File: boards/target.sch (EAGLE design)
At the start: 20 parts, among them Q1 BC847BS, U1 MCP1703T-3002E/CB, X1 53398-04, X2 53398-04

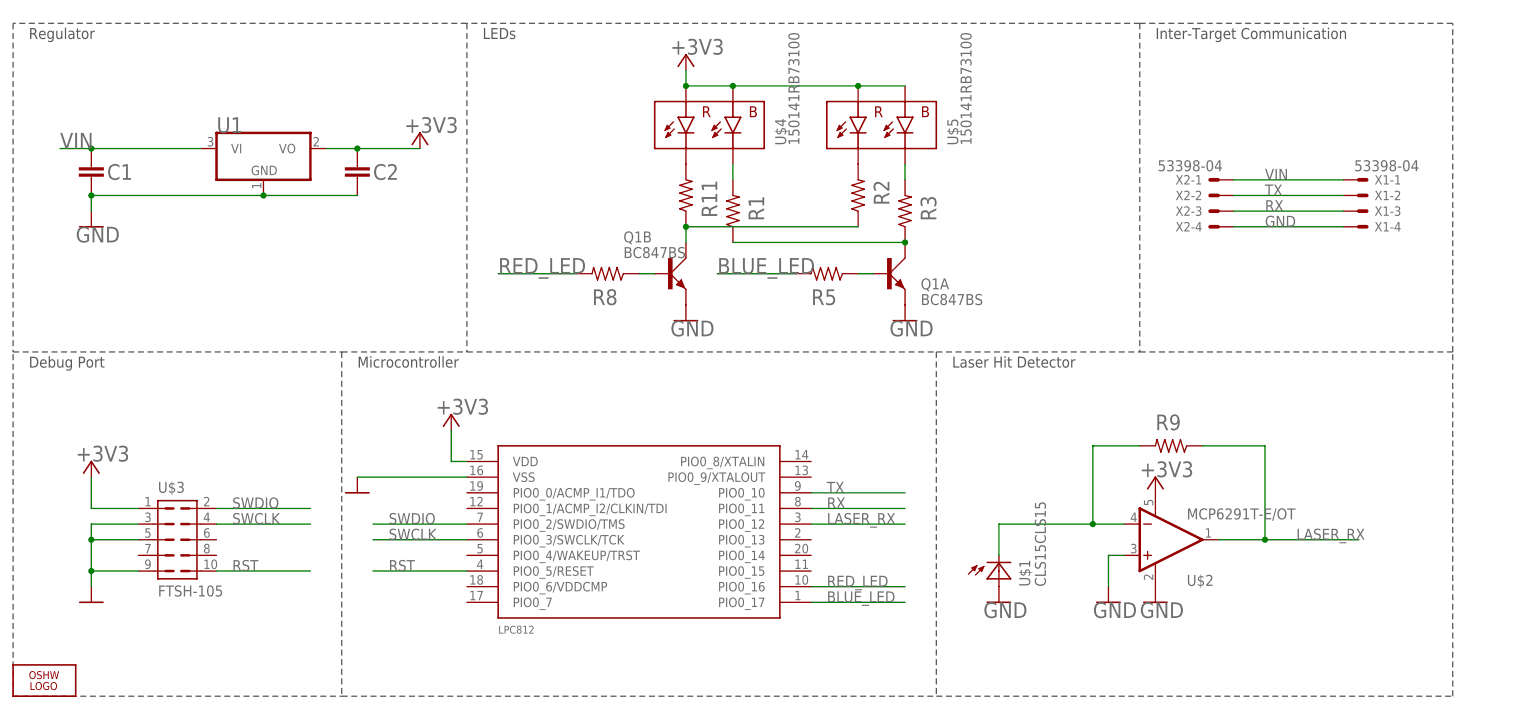
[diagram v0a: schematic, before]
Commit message: Rename to target.sch/brd. Fix controller. Add part numbers. Still needs to be routed.
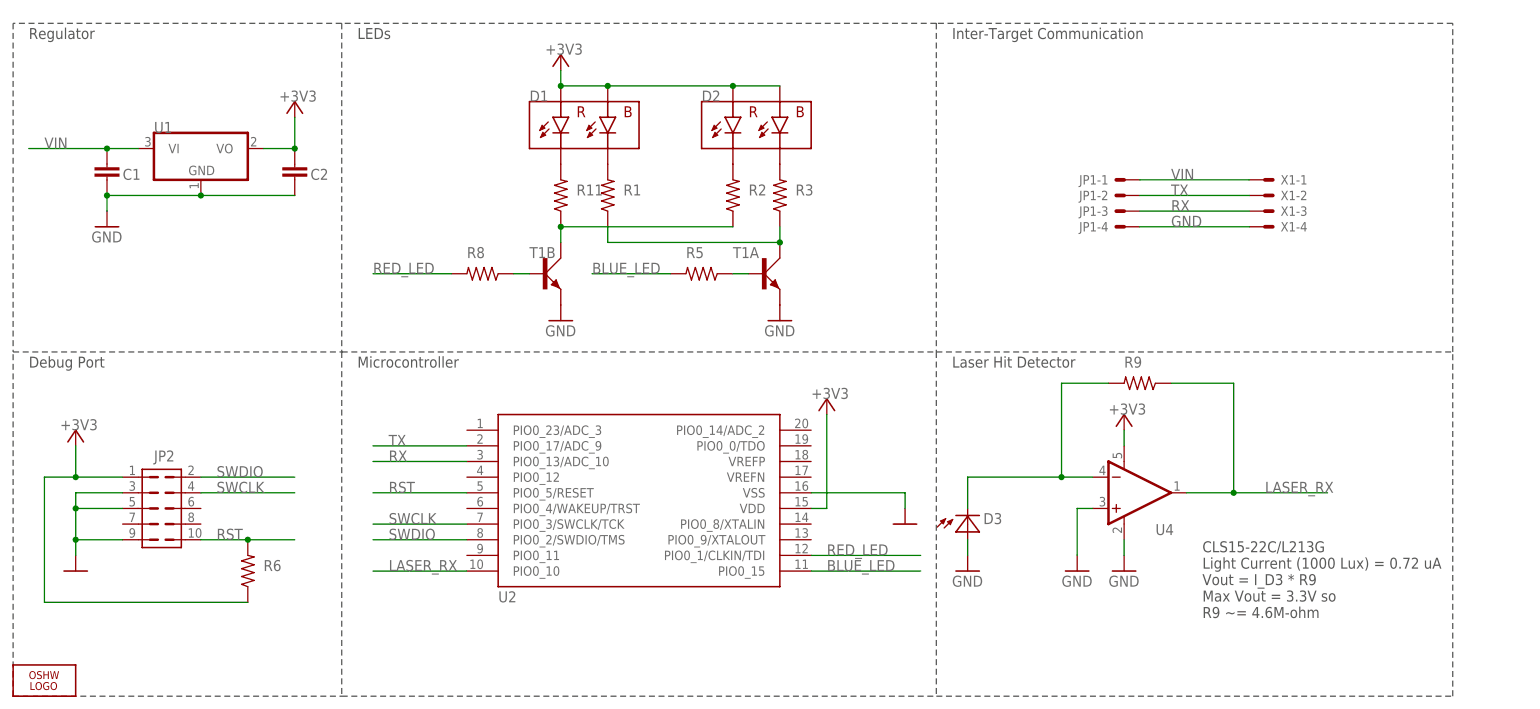
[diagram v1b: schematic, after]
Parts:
- removed LPC812: LPC812M101JDH20, LPC800:LPC812M101JDH20
- removed Q1: BC847BS, transistor-small-signal:BC847BS
- removed U$1: CLS15CLS15, torpedo:CLS15CLS15
- removed U$2: MCP6291T-E/OT, SparkFun-AnalogIC:MCP6291T-E/OT
- removed U$3: FTSH-105, torpedo:FTSH-105
- removed U$4, U$5: 150141RB73100, torpedo:LED_RB
- removed X2: 53398-04, con-molex:53398-04
- added D1, D2: 150141RB73100, torpedo:LED_RB
- added D3: 638-CLS1522CL213GTR8, torpedo:CLS15CLS15
- added JP1: 798-DF134P125V20, con-molex:53398-04
- added JP2: FTSH-105-01-L, torpedo:FTSH-105
- added R6: 71-CRCW0603-10K-E3, rcl:R-US_R0603
- added T1: 771-BC847BS-T/R, transistor-small-signal:BC847BS
- added U2: 771-LPC824M201JDH20J, torpedo:LPC824
- added U4: 579-MCP6291T-E/OT, SparkFun-AnalogIC:MCP6291T-E/OT
- R1, R3: value CRCW0603200RFKEA -> 71-CRCW0603-5.6-E3
- R11, R2: value CRCW0603200RFKEA -> 71-CRCW060368R0FKEB
- R5, R8: value CRCW0603200RFKEA -> 71-CRCW0603220RFKEB
- R9: value CRCW0603200RFKEA -> 71-CRCW06034M64FKEA
- U1: value MCP1703T-3002E/CB -> 579-MCP1703T-3002ECB
- X1: value 53398-04 -> 798-DF134P125V20
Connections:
- net +3V3: now also D1.1, D1.2, D2.1, D2.2, JP2.1, R6.1, U2.VDD, U4.V+; no longer LPC812.VDD, U$2.V+, U$3.1, U$4.1, U$4.2, U$5.1, U$5.2
- net BLUE_LED: now also U2.PIO0_15; no longer LPC812.PIO0_17
- net GND: now also D3.A, JP1-4.S, JP2.3, JP2.5, JP2.9, T1A.E, T1B.E, U2.VSS, U4.+IN, U4.V-; no longer LPC812.VSS, Q1A.E, Q1B.E, U$1.A, U$2.+IN, U$2.V-, U$3.3, U$3.5, U$3.9, X2-4.S
- net LASER_RX: now also U2.PIO0_10, U4.OUT; no longer LPC812.PIO0_12, U$2.OUT
- net N$1: now also T1A.C; no longer Q1A.C
- net N$11: now also T1B.B; no longer Q1B.B
- net N$2: now also T1B.C; no longer Q1B.C
- net N$3: now also D1.3; no longer U$4.3
- net N$4: now also T1A.B; no longer Q1A.B
- net N$5: now also D3.C, U4.-IN; no longer U$1.C, U$2.-IN
- net N$6: now also D2.3; no longer U$5.3
- net N$7: now also D1.4; no longer U$4.4
- net N$8: now also D2.4; no longer U$5.4
- net RED_LED: now also U2.PIO0_1/CLKIN/TDI; no longer LPC812.PIO0_16
- net RST: now also JP2.10, R6.2, U2.PIO0_5/RESET; no longer LPC812.PIO0_5/RESET, U$3.10
- net RX: now also JP1-3.S, U2.PIO0_13/ADC_10; no longer LPC812.PIO0_11, X2-3.S
- net SWCLK: now also JP2.4, U2.PIO0_3/SWCLK/TCK; no longer LPC812.PIO0_3/SWCLK/TCK, U$3.4
- net SWDIO: now also JP2.2, U2.PIO0_2/SWDIO/TMS; no longer LPC812.PIO0_2/SWDIO/TMS, U$3.2
- net TX: now also JP1-2.S, U2.PIO0_17/ADC_9; no longer LPC812.PIO0_10, X2-2.S
- net VIN: now also JP1-1.S; no longer X2-1.S
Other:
- note added: "CLS15-22C/L213G Light Current (1000 Lux) = 0.72 uA Vout = I_D3 * R9 Max Vout = 3.3V so R9 ~= 4.6M-ohm"
- moved on the sheet: C1, C2, R1, R11, R2, R3, R5, R8, R9, U1, X1-1, X1-2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

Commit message: Working on target layout
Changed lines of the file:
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@@
 <part name="JP2" library="torpedo" deviceset="FTSH-105" device="" value="FTSH-105-01-L"/>
 <part name="R6" library="rcl" deviceset="R-US_" device="R0603" value="71-CRCW0603-10K-E3"/>
+<part name="GND3" library="supply1" deviceset="GND" device=""/>
+<part name="GND10" library="supply1" deviceset="GND" device=""/>
 </parts>
 <sheets>
@@
 <attribute name="NAME" x="40.64" y="20.32" size="1.778" layer="95"/>
 </instance>
+<instance part="GND3" gate="1" x="30.48" y="76.2" smashed="yes">
+<attribute name="VALUE" x="27.94" y="73.66" size="1.778" layer="96"/>
+</instance>
+<instance part="GND10" gate="1" x="45.72" y="76.2" smashed="yes">
+<attribute name="VALUE" x="43.18" y="73.66" size="1.778" layer="96"/>
+</instance>
 </instances>
 <busses>
@@
 <net name="GND" class="0">
 <segment>
+<pinref part="C1" gate="G$1" pin="2"/>
 <pinref part="GND1" gate="1" pin="GND"/>
 <wire x1="15.24" y1="78.74" x2="15.24" y2="81.28" width="0.1524" layer="91"/>
-<pinref part="U1" gate="G$1" pin="GND"/>
-<wire x1="15.24" y1="81.28" x2="30.48" y2="81.28" width="0.1524" layer="91"/>
-<pinref part="C1" gate="G$1" pin="2"/>
-<junction x="15.24" y="81.28"/>
-<pinref part="C2" gate="G$1" pin="2"/>
-<wire x1="30.48" y1="81.28" x2="45.72" y2="81.28" width="0.1524" layer="91"/>
-<junction x="30.48" y="81.28"/>
 </segment>
 <segment>
@@
 <junction x="10.16" y="25.4"/>
 </segment>
+<segment>
+<pinref part="U1" gate="G$1" pin="GND"/>
+<pinref part="GND3" gate="1" pin="GND"/>
+<wire x1="30.48" y1="81.28" x2="30.48" y2="78.74" width="0.1524" layer="91"/>
+</segment>
+<segment>
+<pinref part="C2" gate="G$1" pin="2"/>
+<pinref part="GND10" gate="1" pin="GND"/>
+<wire x1="45.72" y1="81.28" x2="45.72" y2="78.74" width="0.1524" layer="91"/>
+</segment>
 </net>

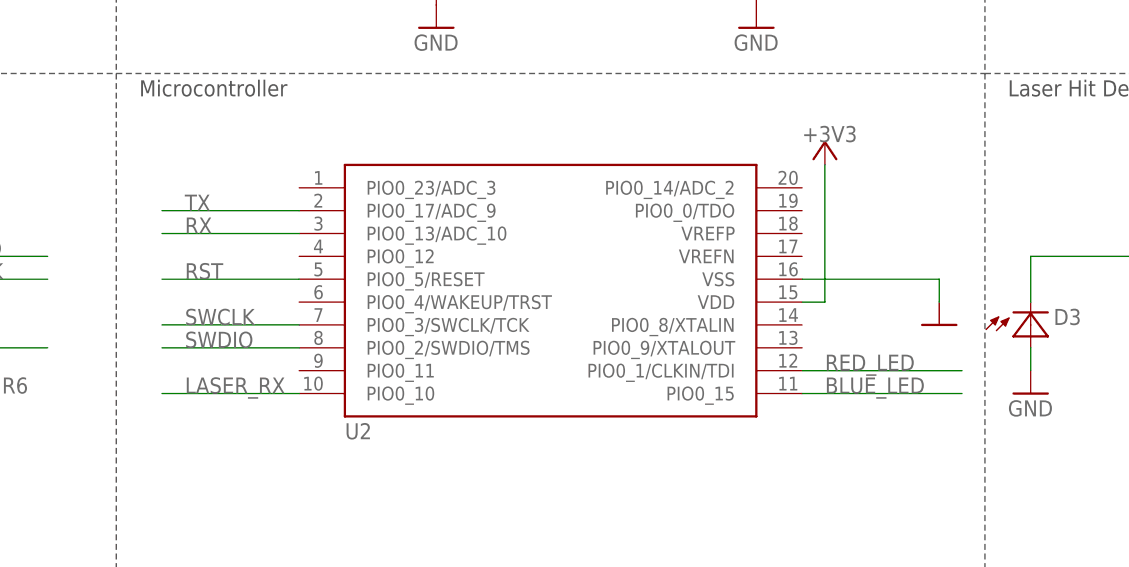
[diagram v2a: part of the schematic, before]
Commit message: First pass target route
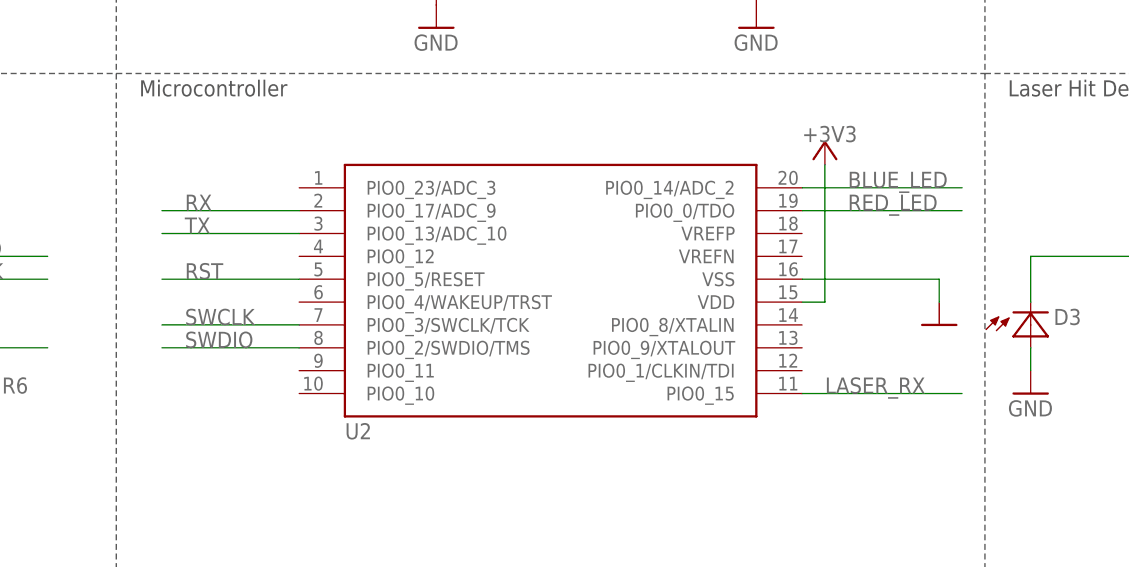
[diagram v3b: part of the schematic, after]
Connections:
- net BLUE_LED: now also U2.PIO0_14/ADC_2; no longer U2.PIO0_15
- net LASER_RX: now also U2.PIO0_15; no longer U2.PIO0_10
- net RED_LED: now also U2.PIO0_0/TDO; no longer U2.PIO0_1/CLKIN/TDI
- net RX: now also U2.PIO0_17/ADC_9; no longer U2.PIO0_13/ADC_10
- net TX: now also U2.PIO0_13/ADC_10; no longer U2.PIO0_17/ADC_9
